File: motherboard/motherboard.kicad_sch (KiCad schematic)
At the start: 39 parts, among them J1 Raspberry_Pi_2_3 ANT, J11 Control Board, J12 coding, J14 USB_C_Receptacle_USB2.0, J2 shaftencorder, J3 c02 censor, J4 Battery / Pitot/ Orientation, J5 lidar, J7 SparLoad, SW1 MCU_RST, U2 AZ1117-3.3, U2 STM32F412RETx, U3 DPS310 - barometer, U4 GPS module, U5 nRF24L01-telemetry, U6 DHT11(DHT22), U7 Bluetooth Module - Shaft Power, U8 Bluetooth Module - Power Cont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, Y1 8M

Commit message: Final motherboard schematic draft
Made several small changes to the schematic:

- Merged all custom symbols into one library
- Touched up custom symbols for aesthetics and organization
- Adjusted schematic for revised schematics
- Added OneWire hardware to schematic
- Removed redudant 3.3V regulator (3.3V will be supplied by control board)
- Improved schematic labelling consistency
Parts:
- removed C7: 10uF, Capacitor_THT:CP_Radial_D5.0mm_P2.00mm, symbol Device:C_Polarized_Small_US
- removed C8: 22uF, Capacitor_THT:CP_Radial_D5.0mm_P2.00mm, symbol Device:C_Polarized_Small_US
- removed J12: coding, symbol Connector:Conn_01x02_Pin
- removed U2: AZ1117-3.3, Package_TO_SOT_SMD:SOT-223-3_TabPin2, symbol Regulator_Linear:AZ1117-3.3
- removed U3: DPS310 - barometer, Package_LGA:Bosch_LGA-8_2x2.5mm_P0.65mm_ClockwisePinNumbering, symbol mb_sensors:DPS310
- added C11, C12: 100n, symbol Device:C
- added J2: PROGRAM, symbol Connector:Conn_01x04_Pin
- added Q1: 2N7002K, Package_TO_SOT_SMD:SOT-23, symbol Transistor_FET:2N7002K
- added R9: 5.6k, Resistor_SMD:R_0603_1608Metric, symbol Device:R_US
- added U9: DPS310 - barometer, Package_LGA:Bosch_LGA-8_2x2.5mm_P0.65mm_ClockwisePinNumbering, symbol mb_sensors:DPS310
- C1: renamed from C9; value 10nf -> 10n
- U2: renamed from IMU6axis; value ~ -> IMU; footprint (none) -> Package_LGA:LGA-14_3x2.5mm_P0.5mm_LayoutBorder3x4y
- U4: symbol mb_MT3339:MT3339 -> mb_sensors:MT3339
- renumbered C10 to C2, J4 to J3, J3 to J4, J2 to J5, J5 to J8, J11 to J9, R7 to R1, R8 to R3, U7 to U1, U8 to U3, U6 to U5, U2 to U6, U5 to U8
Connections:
- net tele_ce is gone; now on net TELE_{CE}: U8.3 (CE)
- net tele_cs is gone; now on net TELE_{CS}: U8.4 (~{CSN})
- net tele_irq is gone; now on net TELE_{IRQ}: U8.8 (IRQ)
- net +3.3V: now also C11.1, C12.1, J2.4 (Pin_4), U9.6 (V_{DDIO}), U9.8 (V_{DD})
- net +5V: now also R9.1
- net GND: now also U2.10 (RESV), U2.2 (RESV), U2.3 (RESV), C11.2, C12.2, J2.1 (Pin_1), Q1.2 (S), U9.1 (GND), U9.7 (GND)
- net I2C_{SCK}: now also U9.4 (SCK)
- net I2C_{SDA}: now also U9.3 (SDI)
- net OneWire_{RX}: now reaches U6.10 (PC2)
- net OneWire_{RX}: now also J7.2 (Pin_2), Q1.3 (D), R9.2
- net SWDIO: now reaches U6.2 (PC13)
- net SWDIO: now also J2.2 (Pin_2)
- net SWCLK: now reaches U6.3 (PC14)
- net SWCLK: now also J2.3 (Pin_3)
- net TELE_{CS}: now reaches U6.41 (PA8)
- net TELE_{CE}: now reaches U6.42 (PA9)
- net TELE_{IRQ}: now reaches U6.43 (PA10)
- net C_{O2} renamed CO_{2}
- net IMU_cs renamed IMU_{CS}
- net IMU_{CS}: no longer U2.4 (INT)
- net SparLoad renamed OneWire_{TX}
- net OneWire_{TX}: now also Q1.1 (G); no longer J7.2 (Pin_2)
- net USART3RX renamed USART3_{RX}
- net USART3TX renamed USART3_{TX}
- net USART6RX renamed USART6_{RX}
- net USART6TX renamed USART6_{TX}
- no-connect marks 36 -> 61
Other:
- company: (none) -> HPVDT
- title: (none) -> Falcon Motherboard
- moved on the sheet: C1, C2, J5, J7, R3

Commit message: FootPrints assigned
Assigned resistor and capacitor footprints
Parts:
- C1, C11, C12, C2: footprint (none) -> Capacitor_SMD:C_0603_1608Metric
- R1, R3: footprint (none) -> Resistor_SMD:R_0603_1608Metric
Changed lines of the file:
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@@
       (effects (font (size 1.27 1.27)) (justify left))
     )
-    (property "Footprint" "" (at 48.5648 208.28 0)
+    (property "Footprint" "Capacitor_SMD:C_0603_1608Metric" (at 48.5648 208.28 0)
       (effects (font (size 1.27 1.27)) hide)
     )
@@
       (effects (font (size 1.27 1.27)))
     )
-    (property "Footprint" "" (at 170.434 249.174 90)
+    (property "Footprint" "Resistor_SMD:R_0603_1608Metric" (at 170.434 249.174 90)
       (effects (font (size 1.27 1.27)) hide)
     )
@@
       (effects (font (size 1.27 1.27)) (justify left))
     )
-    (property "Footprint" "" (at 370.5352 218.44 0)
+    (property "Footprint" "Capacitor_SMD:C_0603_1608Metric" (at 370.5352 218.44 0)
       (effects (font (size 1.27 1.27)) hide)
     )
@@
       (effects (font (size 1.27 1.27)) (justify left))
     )
-    (property "Footprint" "" (at 362.2548 218.44 0)
+    (property "Footprint" "Capacitor_SMD:C_0603_1608Metric" (at 362.2548 218.44 0)
       (effects (font (size 1.27 1.27)) hide)
     )
@@
       (effects (font (size 1.27 1.27)) (justify right))
     )
-    (property "Footprint" "" (at 187.6552 143.51 0)
+    (property "Footprint" "Capacitor_SMD:C_0603_1608Metric" (at 187.6552 143.51 0)
       (effects (font (size 1.27 1.27)) hide)
     )
@@
       (effects (font (size 1.27 1.27)) (justify left))
     )
-    (property "Footprint" "" (at 194.056 139.446 90)
-      (effects (font (size 1.27 1.27)) hide)
-    )
+    (property "Footprint" "Resistor_SMD:R_0603_1608Metric" (at 194.056 139.446 90)
+      (effects (font (size 1.27 1.27)) hide)
+    )

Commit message: Completed Footprint Draft
Added pin headers for all the remaining components on the board.
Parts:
- J1: footprint (none) -> Connector_PinSocket_2.54mm:PinSocket_2x20_P2.54mm_Vertical
- J2: footprint (none) -> Connector_PinSocket_2.54mm:PinSocket_1x04_P2.54mm_Vertical
- J3, J8: footprint (none) -> Connector_JST:JST_EH_B4B-EH-A_1x04_P2.50mm_Vertical
- J4, J5, J7: footprint (none) -> Connector_JST:JST_EH_B3B-EH-A_1x03_P2.50mm_Vertical
- J9: footprint (none) -> Connector_JST:JST_EH_B5B-EH-A_1x05_P2.50mm_Vertical
- U1, U3: footprint (none) -> Connector_PinSocket_2.54mm:PinSocket_1x06_P2.54mm_Vertical
- U4: footprint (none) -> Connector_PinSocket_2.54mm:PinSocket_1x09_P2.54mm_Vertical
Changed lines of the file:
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@@
       (effects (font (size 1.27 1.27)) (justify right))
     )
-    (property "Footprint" "" (at 401.32 115.57 0)
+    (property "Footprint" "Connector_JST:JST_EH_B4B-EH-A_1x04_P2.50mm_Vertical" (at 401.32 115.57 0)
       (effects (font (size 1.27 1.27)) hide)
     )
@@
       (effects (font (size 1.27 1.27)) (justify right))
     )
-    (property "Footprint" "" (at 353.06 124.46 0)
+    (property "Footprint" "Connector_JST:JST_EH_B4B-EH-A_1x04_P2.50mm_Vertical" (at 353.06 124.46 0)
       (effects (font (size 1.27 1.27)) hide)
     )
@@
       (effects (font (size 1.27 1.27)) (justify left))
     )
-    (property "Footprint" "" (at 58.42 66.04 0)
+    (property "Footprint" "Connector_PinSocket_2.54mm:PinSocket_2x20_P2.54mm_Vertical" (at 58.42 66.04 0)
       (effects (font (size 1.27 1.27)) hide)
     )
@@
       (effects (font (size 1.27 1.27)) (justify left))
     )
-    (property "Footprint" "" (at 85.09 149.86 0)
+    (property "Footprint" "Connector_PinSocket_2.54mm:PinSocket_1x06_P2.54mm_Vertical" (at 85.09 149.86 0)
       (effects (font (size 1.27 1.27)) hide)
     )
@@
       (effects (font (size 1.27 1.27)))
     )
-    (property "Footprint" "" (at 105.41 229.87 0)
+    (property "Footprint" "Connector_PinSocket_2.54mm:PinSocket_1x09_P2.54mm_Vertical" (at 105.41 229.87 0)
       (effects (font (size 1.27 1.27)) hide)
     )
@@
       (effects (font (size 1.27 1.27)) (justify left))
     )
-    (property "Footprint" "" (at 38.1 134.62 0)
+    (property "Footprint" "Connector_PinSocket_2.54mm:PinSocket_1x06_P2.54mm_Vertical" (at 38.1 134.62 0)
       (effects (font (size 1.27 1.27)) hide)
     )
@@
       (effects (font (size 1.27 1.27)))
     )
-    (property "Footprint" "" (at 349.25 76.2 0)
+    (property "Footprint" "Connector_JST:JST_EH_B3B-EH-A_1x03_P2.50mm_Vertical" (at 349.25 76.2 0)
       (effects (font (size 1.27 1.27)) hide)
     )
@@
       (effects (font (size 1.27 1.27)) (justify right))
     )
-    (property "Footprint" "" (at 384.81 177.8 0)
+    (property "Footprint" "Connector_JST:JST_EH_B3B-EH-A_1x03_P2.50mm_Vertical" (at 384.81 177.8 0)
       (effects (font (size 1.27 1.27)) hide)
     )
@@
       (effects (font (size 1.27 1.27)) (justify right))
     )
-    (property "Footprint" "" (at 345.44 166.37 0)
+    (property "Footprint" "Connector_PinSocket_2.54mm:PinSocket_1x04_P2.54mm_Vertical" (at 345.44 166.37 0)
       (effects (font (size 1.27 1.27)) hide)
     )
@@
       (effects (font (size 1.27 1.27)) (justify right))
     )
-    (property "Footprint" "" (at 401.32 146.05 0)
+    (property "Footprint" "Connector_JST:JST_EH_B5B-EH-A_1x05_P2.50mm_Vertical" (at 401.32 146.05 0)
       (effects (font (size 1.27 1.27)) hide)
     )
@@
       (effects (font (size 1.27 1.27)) (justify right))
     )
-    (property "Footprint" "" (at 372.11 97.79 0)
-      (effects (font (size 1.27 1.27)) hide)
-    )
+    (property "Footprint" "Connector_JST:JST_EH_B3B-EH-A_1x03_P2.50mm_Vertical" (at 372.11 97.79 0)
+      (effects (font (size 1.27 1.27)) hide)
+    )

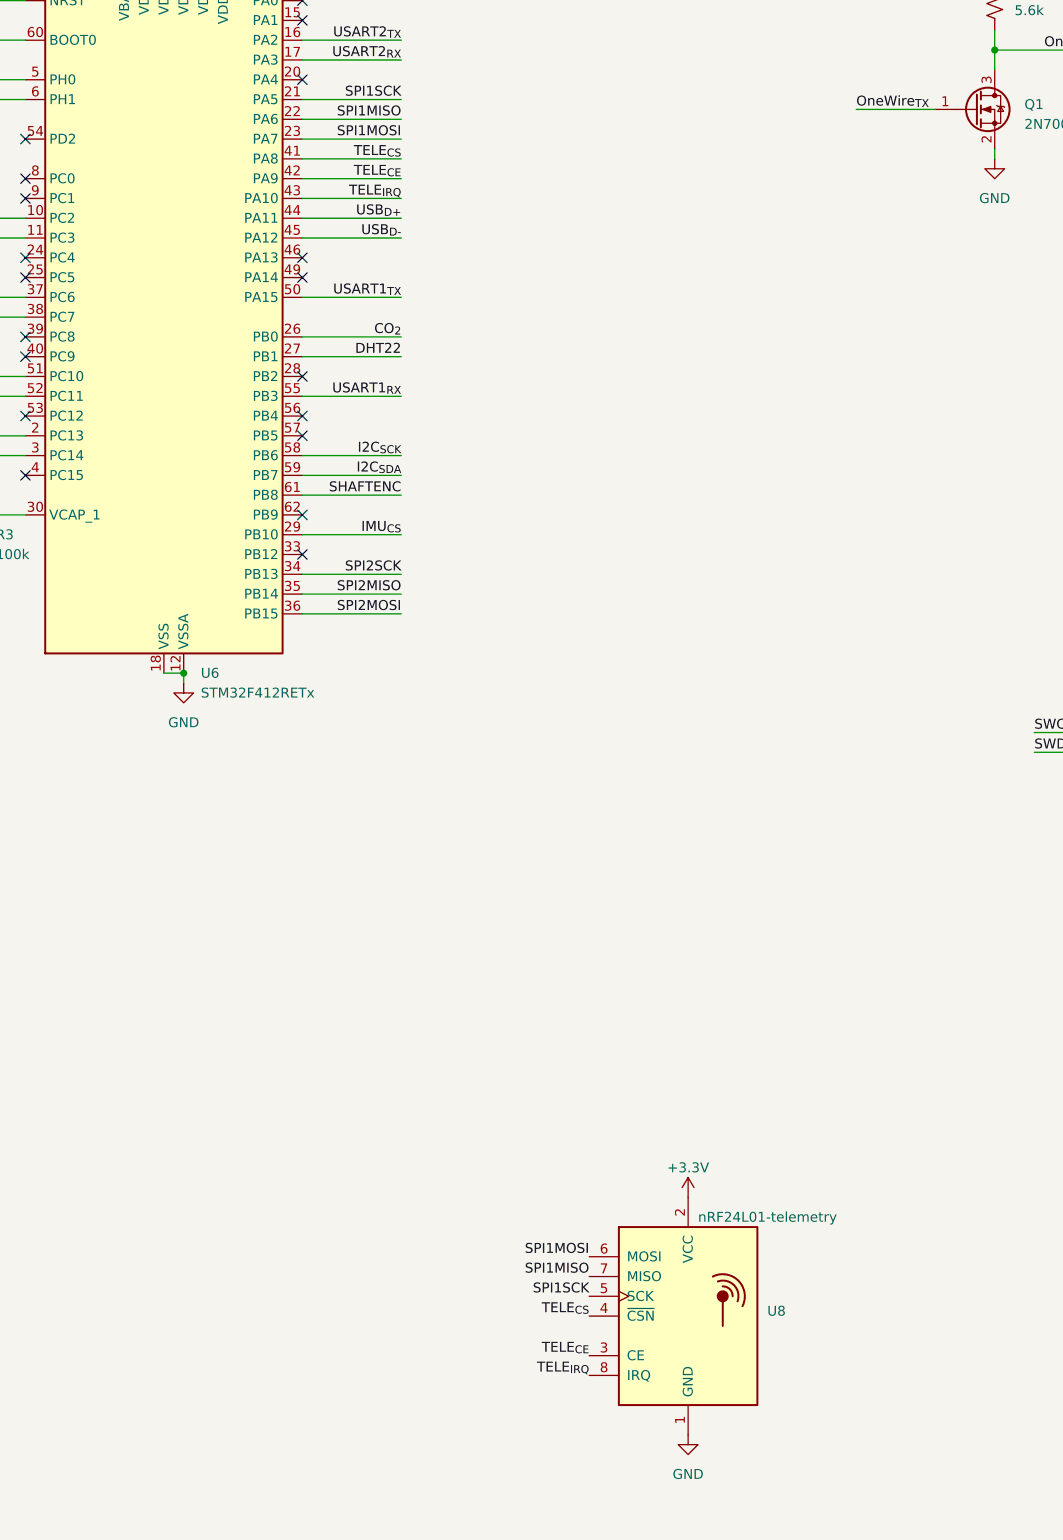
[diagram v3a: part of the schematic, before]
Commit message: Edited footprints
Edited custom footprints and completed first layout draft
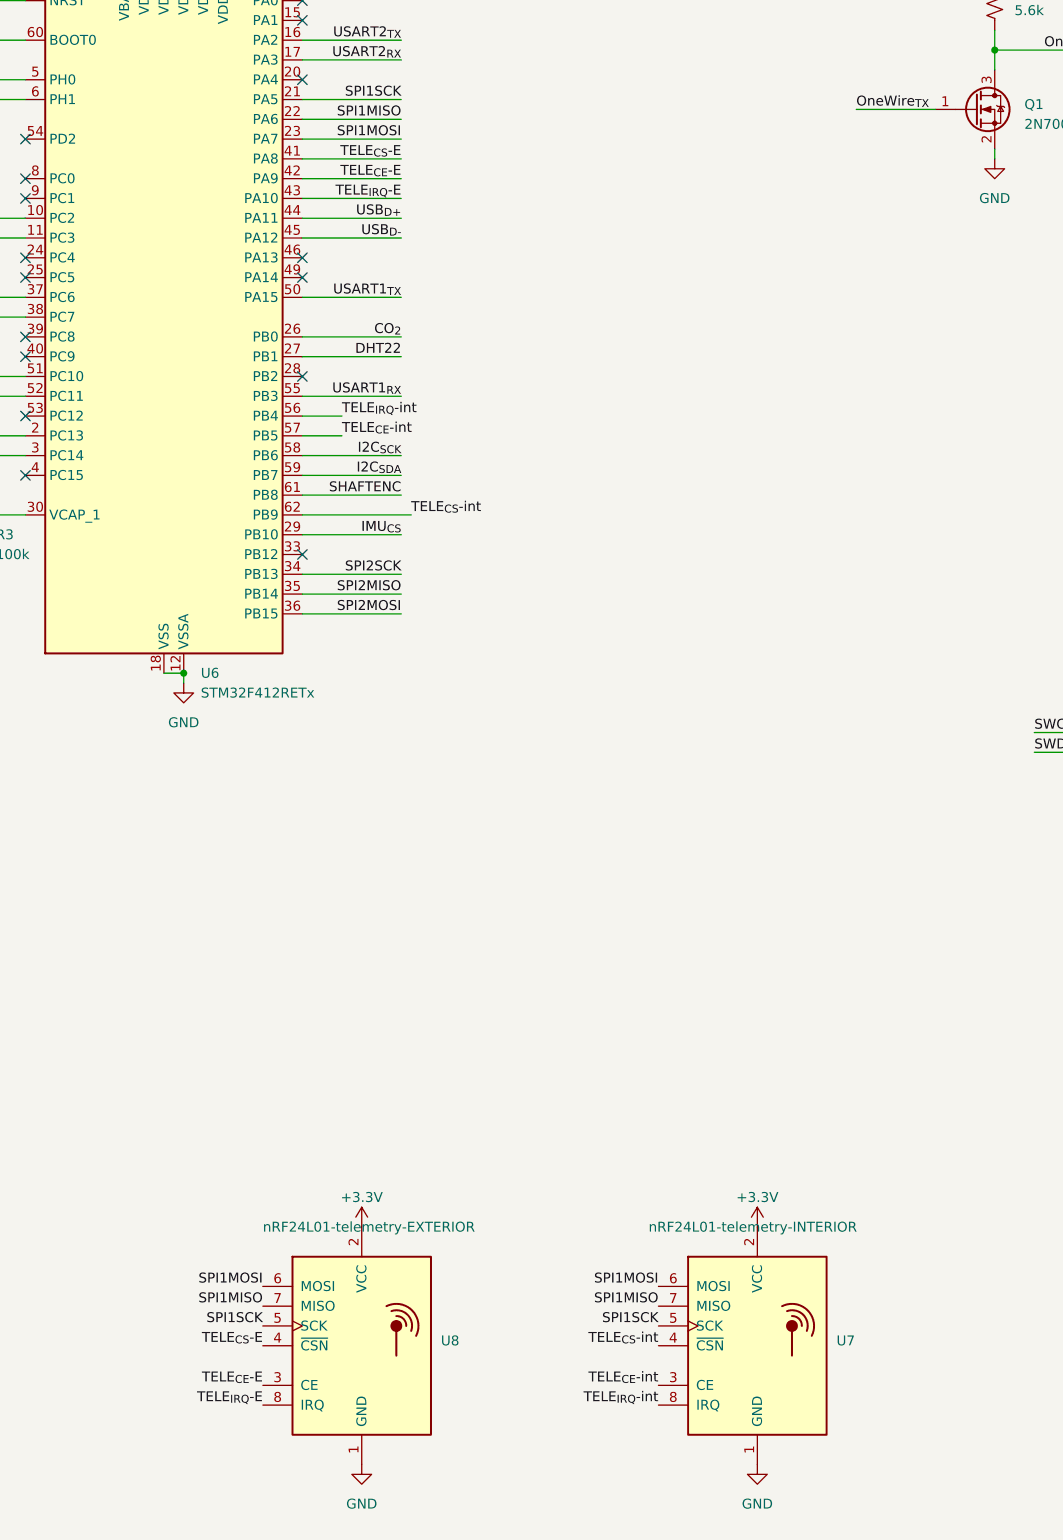
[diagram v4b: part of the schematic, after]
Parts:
- added U7: nRF24L01-telemetry-INTERIOR, RF_Module:nRF24L01_Breakout, symbol RF:NRF24L01_Breakout
- JP1: footprint Connector_PinHeader_2.54mm:PinHeader_1x03_P2.54mm_Vertical -> Jumper:SolderJumper-3_P2.0mm_Open_TrianglePad1.0x1.5mm_NumberLabels
- U8: value nRF24L01-telemetry -> nRF24L01-telemetry-EXTERIOR
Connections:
- net +3.3V: now also U7.2 (VCC)
- net GND: now also U7.1 (GND)
- net SPI1MISO: now also U7.7 (MISO)
- net SPI1MOSI: now also U7.6 (MOSI)
- net SPI1SCK: now also U7.5 (SCK)
- net TELE_{IRQ}-int: now reaches U6.56 (PB4)
- net TELE_{IRQ}-int: now also U7.8 (IRQ)
- net TELE_{CE}-int: now reaches U6.57 (PB5)
- net TELE_{CE}-int: now also U7.3 (CE)
- net TELE_{CS}-int: now reaches U6.62 (PB9)
- net TELE_{CS}-int: now also U7.4 (~{CSN})
- net TELE_{CE} renamed TELE_{CE}-E
- net TELE_{CS} renamed TELE_{CS}-E
- net TELE_{IRQ} renamed TELE_{IRQ}-E
- no-connect marks 61 -> 58
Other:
- moved on the sheet: U8

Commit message: Completed feedback for draft 1 round 1
addded thicker traces, disconnected 3.3V from RPi, changed capacitor location, added mounting holes for RPi, added mounting holes to the board, added programming labels
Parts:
- added H1, H2, H3, H4: MountingHole, MountingHole:MountingHole_2.5mm_Pad, symbol Mechanical:MountingHole
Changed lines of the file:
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@@
+    )
+  )
+  (symbol (lib_id "Mechanical:MountingHole") (at 327.66 218.44 0) (unit 1)
+    (in_bom yes) (on_board yes) (dnp no) (fields_autoplaced)
+    (property "Reference" "H3" (at 330.2 217.805 0)
+      (effects (font (size 1.27 1.27)) (justify left))
+    )
+    (property "Value" "MountingHole" (at 330.2 220.345 0)
+      (effects (font (size 1.27 1.27)) (justify left))
+    )
+    (property "Footprint" "MountingHole:MountingHole_2.5mm_Pad" (at 327.66 218.44 0)
+      (effects (font (size 1.27 1.27)) hide)
+    )
+    (property "Datasheet" "~" (at 327.66 218.44 0)
+      (effects (font (size 1.27 1.27)) hide)
+    )
+    (instances
+      (project "motherboard"
+        (path "/39c7ec0f-0a05-4172-b48a-dcc9b63f77ff"
+          (reference "H3") (unit 1)
+        )
+      )
     )
   )
@@
         (path "/4c92aca5-528c-4811-a454-a46e63f9e159"
           (reference "R2") (unit 1)
+        )
+      )
+    )
+  )
+  (symbol (lib_id "Mechanical:MountingHole") (at 327.66 223.52 0) (unit 1)
+    (in_bom yes) (on_board yes) (dnp no) (fields_autoplaced)
+    (property "Reference" "H2" (at 330.2 222.885 0)
+      (effects (font (size 1.27 1.27)) (justify left))
+    )
+    (property "Value" "MountingHole" (at 330.2 225.425 0)
+      (effects (font (size 1.27 1.27)) (justify left))
+    )
+    (property "Footprint" "MountingHole:MountingHole_2.5mm_Pad" (at 327.66 223.52 0)
+      (effects (font (size 1.27 1.27)) hide)
+    )
+    (property "Datasheet" "~" (at 327.66 223.52 0)
+      (effects (font (size 1.27 1.27)) hide)
+    )
+    (instances
+      (project "motherboard"
+        (path "/39c7ec0f-0a05-4172-b48a-dcc9b63f77ff"
+          (reference "H2") (unit 1)
         )
       )
@@
     )
   )
+  (symbol (lib_id "Mechanical:MountingHole") (at 327.66 213.36 0) (unit 1)
+    (in_bom yes) (on_board yes) (dnp no) (fields_autoplaced)
+    (property "Reference" "H4" (at 330.2 212.725 0)
+      (effects (font (size 1.27 1.27)) (justify left))
+    )
+    (property "Value" "MountingHole" (at 330.2 215.265 0)
+      (effects (font (size 1.27 1.27)) (justify left))
+    )
+    (property "Footprint" "MountingHole:MountingHole_2.5mm_Pad" (at 327.66 213.36 0)
+      (effects (font (size 1.27 1.27)) hide)
+    )
+    (property "Datasheet" "~" (at 327.66 213.36 0)
+      (effects (font (size 1.27 1.27)) hide)
+    )
+    (instances
+      (project "motherboard"
+        (path "/39c7ec0f-0a05-4172-b48a-dcc9b63f77ff"
+          (reference "H4") (unit 1)
+        )
+      )
+    )
+  )
   (symbol (lib_id "Device:R_US") (at 360.68 50.8 90) (unit 1)
     (in_bom yes) (on_board yes) (dnp no)
@@
         )
       )
+    )
+  )
+  (symbol (lib_id "Mechanical:MountingHole") (at 327.66 228.6 0) (unit 1)
+    (in_bom yes) (on_board yes) (dnp no) (fields_autoplaced)
+    (property "Reference" "H1" (at 330.2 227.965 0)
+      (effects (font (size 1.27 1.27)) (justify left))
+    )
+    (property "Value" "MountingHole" (at 330.2 230.505 0)
+      (effects (font (size 1.27 1.27)) (justify left))
+    )
+    (property "Footprint" "MountingHole:MountingHole_2.5mm_Pad" (at 327.66 228.6 0)
+      (effects (font (size 1.27 1.27)) hide)
+    )
+    (property "Datasheet" "~" (at 327.66 228.6 0)
+      (effects (font (size 1.27 1.27)) hide)
+    )
+    (instances
+      (project "motherboard"
+        (path "/39c7ec0f-0a05-4172-b48a-dcc9b63f77ff"
+          (reference "H1") (unit 1)
+        )
+      )

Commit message: Minor tweaks to motherboard
- Changed DRC settings to allow tighter copper spacing.
- Removed RPi 3.3V connection
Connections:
- net +3.3V: no longer J1.1 (3V3), J1.17 (3V3)
- no-connect marks 58 -> 60
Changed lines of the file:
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@@
     (company "HPVDT")
-  )
-  (junction (at 63.5 33.02) (diameter 0) (color 0 0 0 0)
   )
   (junction (at 254 58.42) (diameter 0) (color 0 0 0 0)
@@
   (no_connect (at 38.1 78.74))
   (no_connect (at 78.74 78.74))
+  (no_connect (at 60.96 33.02))
   (no_connect (at 38.1 73.66))
   (no_connect (at 85.09 154.94))
@@
   (no_connect (at 78.74 86.36))
   (no_connect (at 78.74 68.58))
+  (no_connect (at 63.5 33.02))
   (no_connect (at 107.95 238.76))
   (no_connect (at 107.95 236.22))
@@
     (stroke (width 0) (type default))
   )
-  (wire (pts (xy 63.5 31.75) (xy 63.5 33.02))
-    (stroke (width 0) (type default))
-  )
   (wire (pts (xy 378.46 44.45) (xy 381 44.45))
     (stroke (width 0) (type default))
@@
   )
   (wire (pts (xy 194.31 60.96) (xy 194.31 62.23))
-    (stroke (width 0) (type default))
-  )
-  (wire (pts (xy 60.96 33.02) (xy 63.5 33.02))
     (stroke (width 0) (type default))
   )
@@
         )
       )
-    )
-  )
-  (symbol (lib_id "power:+3.3V") (at 63.5 31.75 0) (unit 1)
-    (in_bom yes) (on_board yes) (dnp no) (fields_autoplaced)
-    (property "Reference" "#PWR06" (at 63.5 35.56 0)
-      (effects (font (size 1.27 1.27)) hide)
-    )
-    (property "Value" "+3.3V" (at 63.5 27.94 0)
-      (effects (font (size 1.27 1.27)))
-    )
-    (property "Footprint" "" (at 63.5 31.75 0)
-      (effects (font (size 1.27 1.27)) hide)
-    )
-    (property "Datasheet" "" (at 63.5 31.75 0)
-      (effects (font (size 1.27 1.27)) hide)
-    )
-    (pin "1")
-    (instances
-      (project "motherboard"
-        (path "/39c7ec0f-0a05-4172-b48a-dcc9b63f77ff"
-          (reference "#PWR06") (unit 1)
-        )
-      )
